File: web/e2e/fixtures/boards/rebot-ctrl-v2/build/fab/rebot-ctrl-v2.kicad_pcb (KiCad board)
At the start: 4 copper layers, 25 x 25 mm, 57 parts, among them J1 JST-SH 8P (ESC), J2 JST-GH 4P (receiver), J3 USB-C 16P, U1 STM32G431KBU6, U2 LMR36506 buck, U3 XC6206 3.3V, U4 LSM6DSV32X, U5 W25Q128JV 16MB

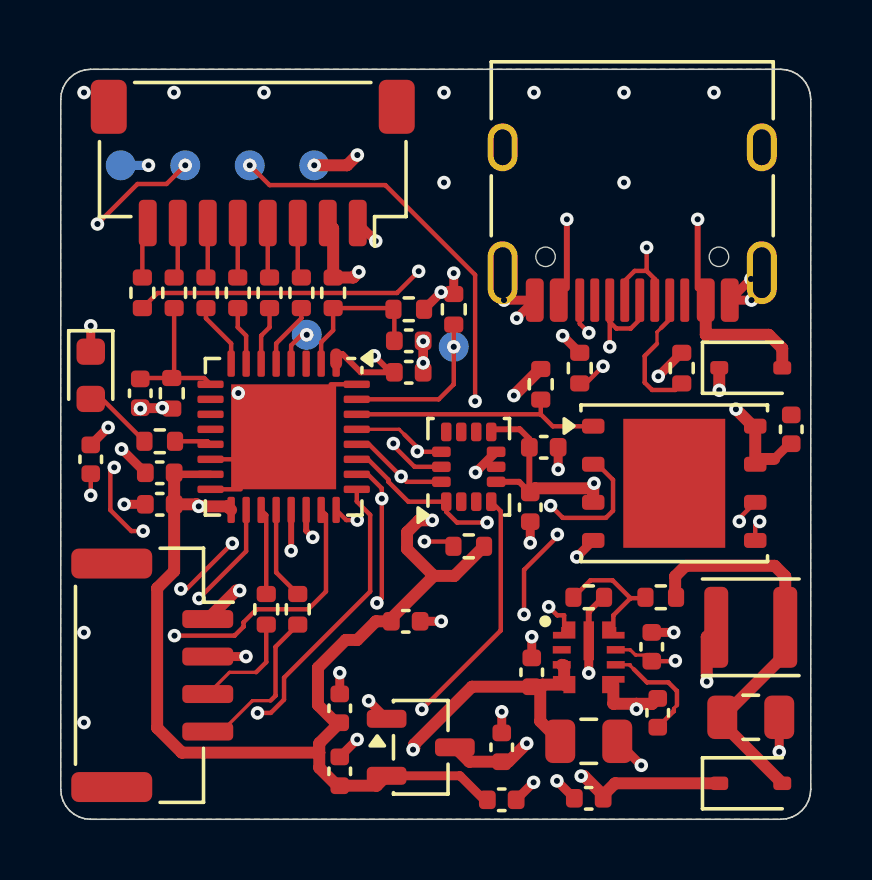
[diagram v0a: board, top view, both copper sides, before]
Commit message: rebot-ctrl-v2e as the default board, with its bottom-silkscreen logo in 2D and 3D
- bundles/rebot-ctrl-v2e (link mode) exported from pcb-lab's fresh build; index.json 'default'
  (exporter --default / make release-bundle DEFAULT=x) opens it; rebot-ctrl-v2 re-exported from its
  rebuild and still in the selector
- board-level silkscreen art (gr_* on F/B.SilkS) in the bundle (Bundle.silkscreen), exporter and
  in-browser importer; drawn filled on the facing side in 2D (Outlines toggle, Bottom view shows
  B.SilkS) and as white art on the board faces in 3D (translucent in X-ray)
- datasheets: LCSC product-page fallback (own productCode only) for parts with no usable cached
  link (GD25Q128E); pin pages indexed from the PDF the viewer shows when LCSC's differs from
  pcb-lab's copy. LSM6DSVE has no LCSC datasheet: LCSC/JLC links only
- fix: no stray hidden #board-name when the board selector is shown (duplicate id after opening a
  local board); tests read counts from pcb-lab reports instead of fixed numbers; fixture regenerated

Co-Authored-By: Claude Opus 5.5 <noreply@anthropic.com>
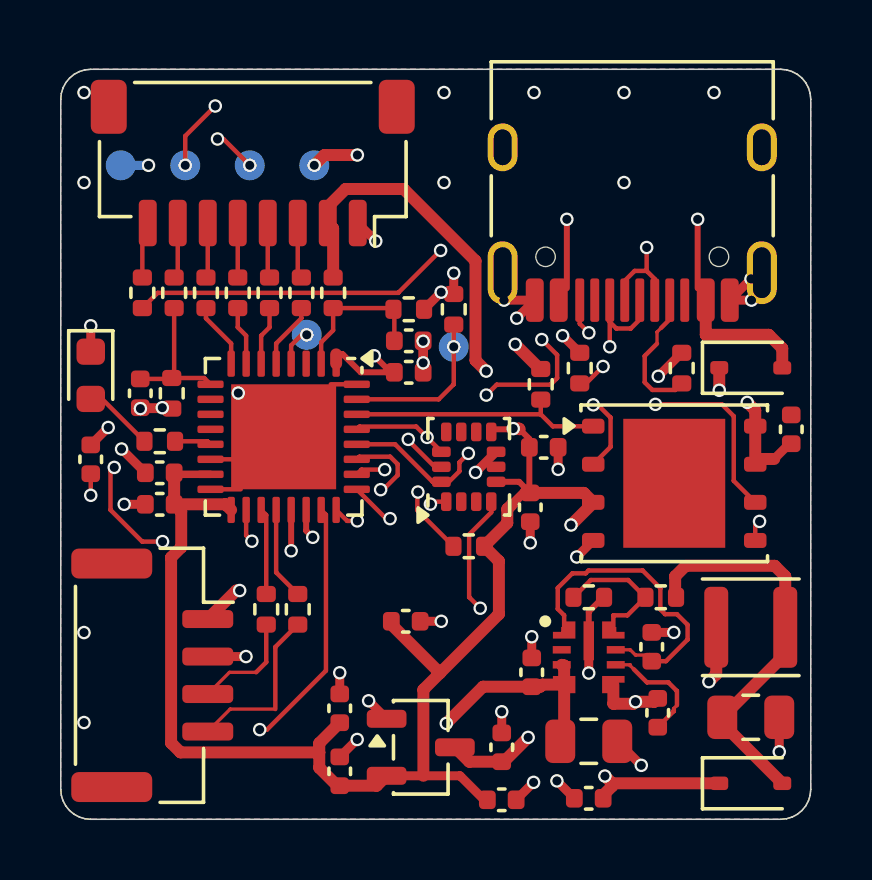
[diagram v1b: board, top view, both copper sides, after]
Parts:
- C17, C18: value 10nF -> 100nF
- U5: value W25Q128JV 16MB -> GD25Q128E 16MB
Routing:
- net VBAT: track 35.2 -> 46.8 mm
- net SWDIO: track 27.7 -> 38.9 mm, vias 5 -> 3
- net IMU_INT1: track 24.2 -> 13.8 mm
- net TLM_RX: track 38.3 -> 32.0 mm
- net 3V3: track 85.7 -> 79.5 mm, vias 8 -> 7
- net SPI_MISO: track 12.1 -> 18.0 mm, vias 2 -> 3
- net SWCLK: track 20.8 -> 26.0 mm, vias 3 -> 5
- net SPI_SCK: track 24.2 -> 21.2 mm, vias 6 -> 3
- net BUCK_VCC: track 8.32 -> 10.6 mm, vias 2 -> 0
- net SPI_MOSI: track 18.8 -> 20.9 mm
- net +5V: track 43.5 -> 45.1 mm
- net GND: vias 47 -> 46
